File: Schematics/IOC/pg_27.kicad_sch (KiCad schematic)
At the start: 18 parts, among them U2801 F64, U2802 F64, U2803 F74, U2804 F74, U2805 F04, U2806 F04, U2807 F04, U2808 F04, U2809 F04, U2810 F04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

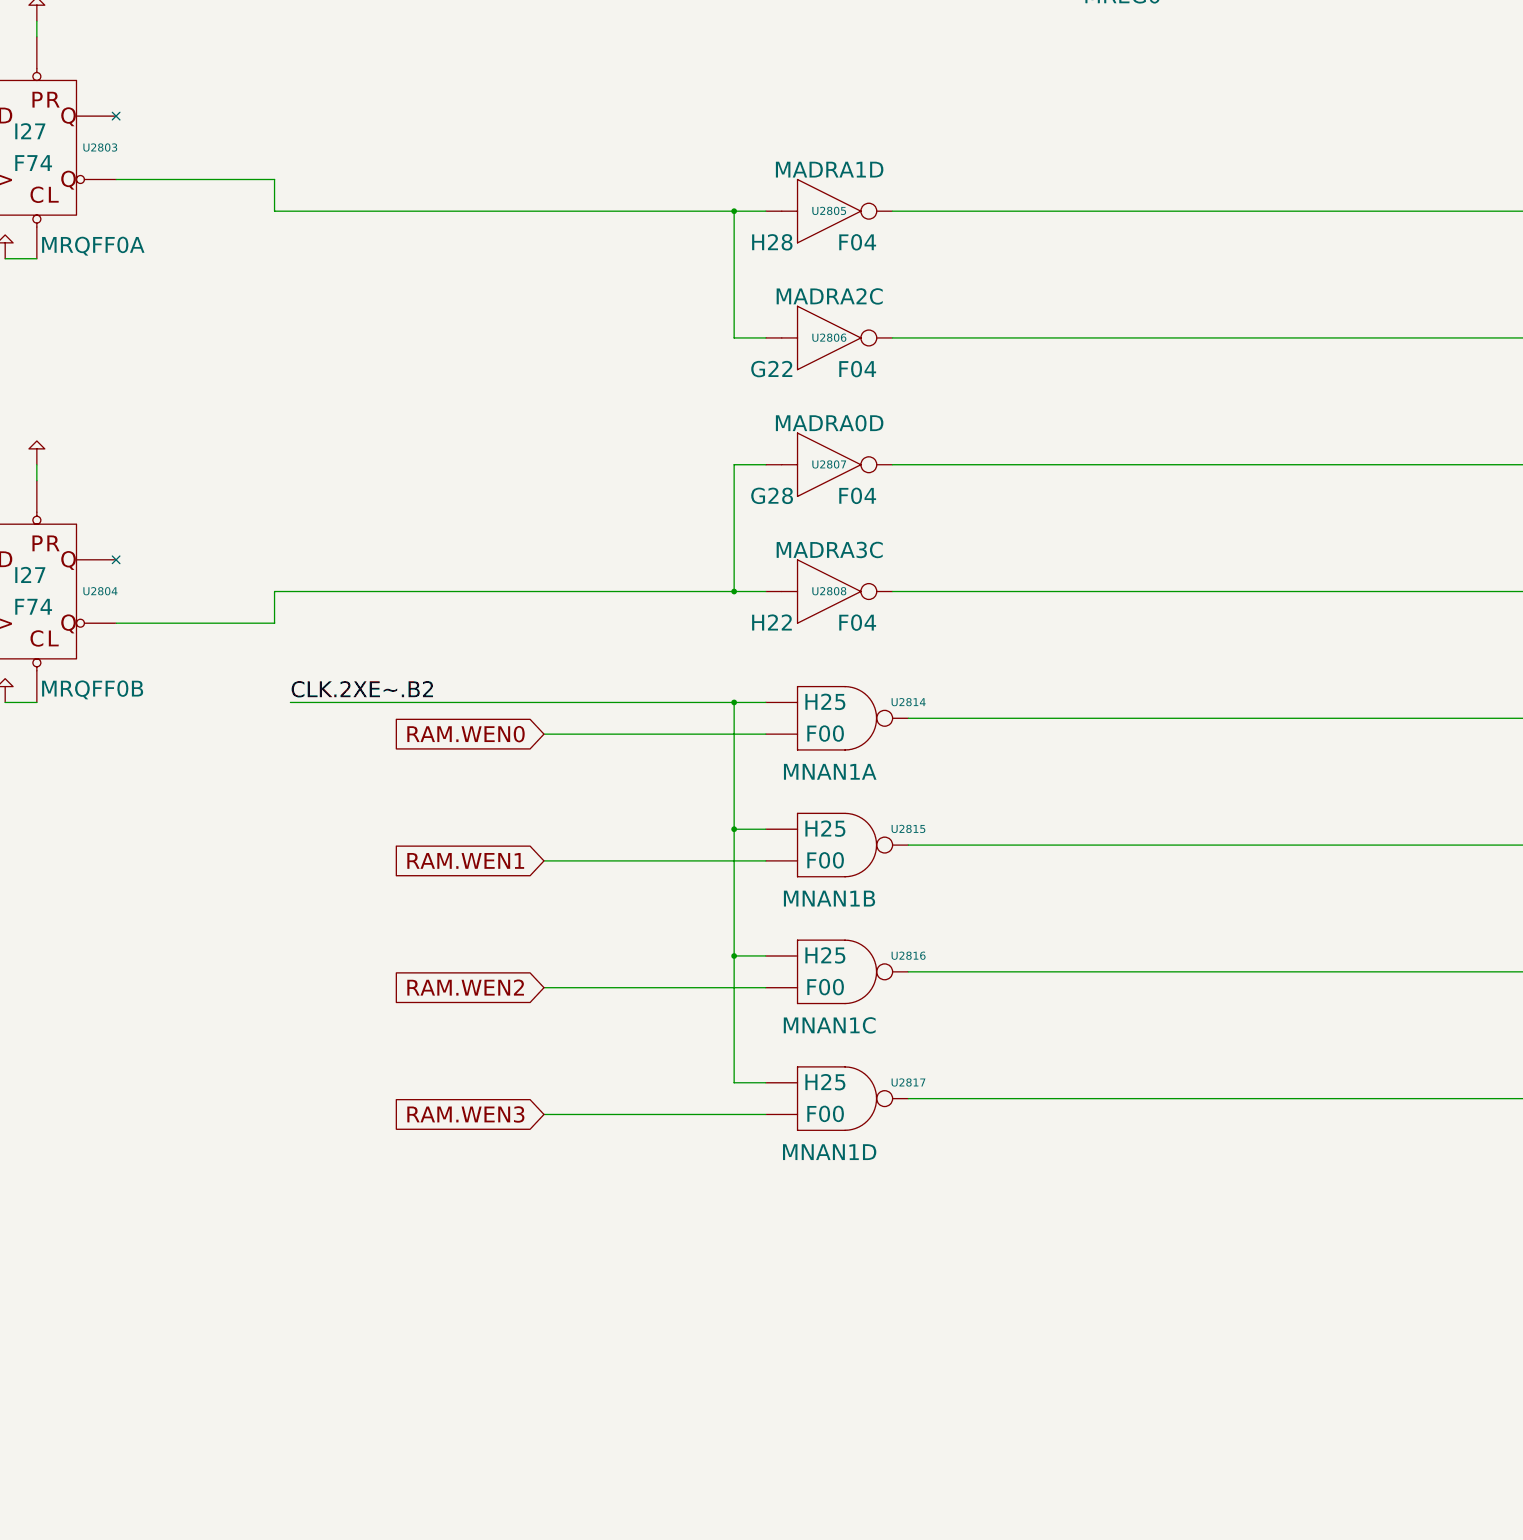
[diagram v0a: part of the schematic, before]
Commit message: Add workarounds necessary for SystemC simulation.
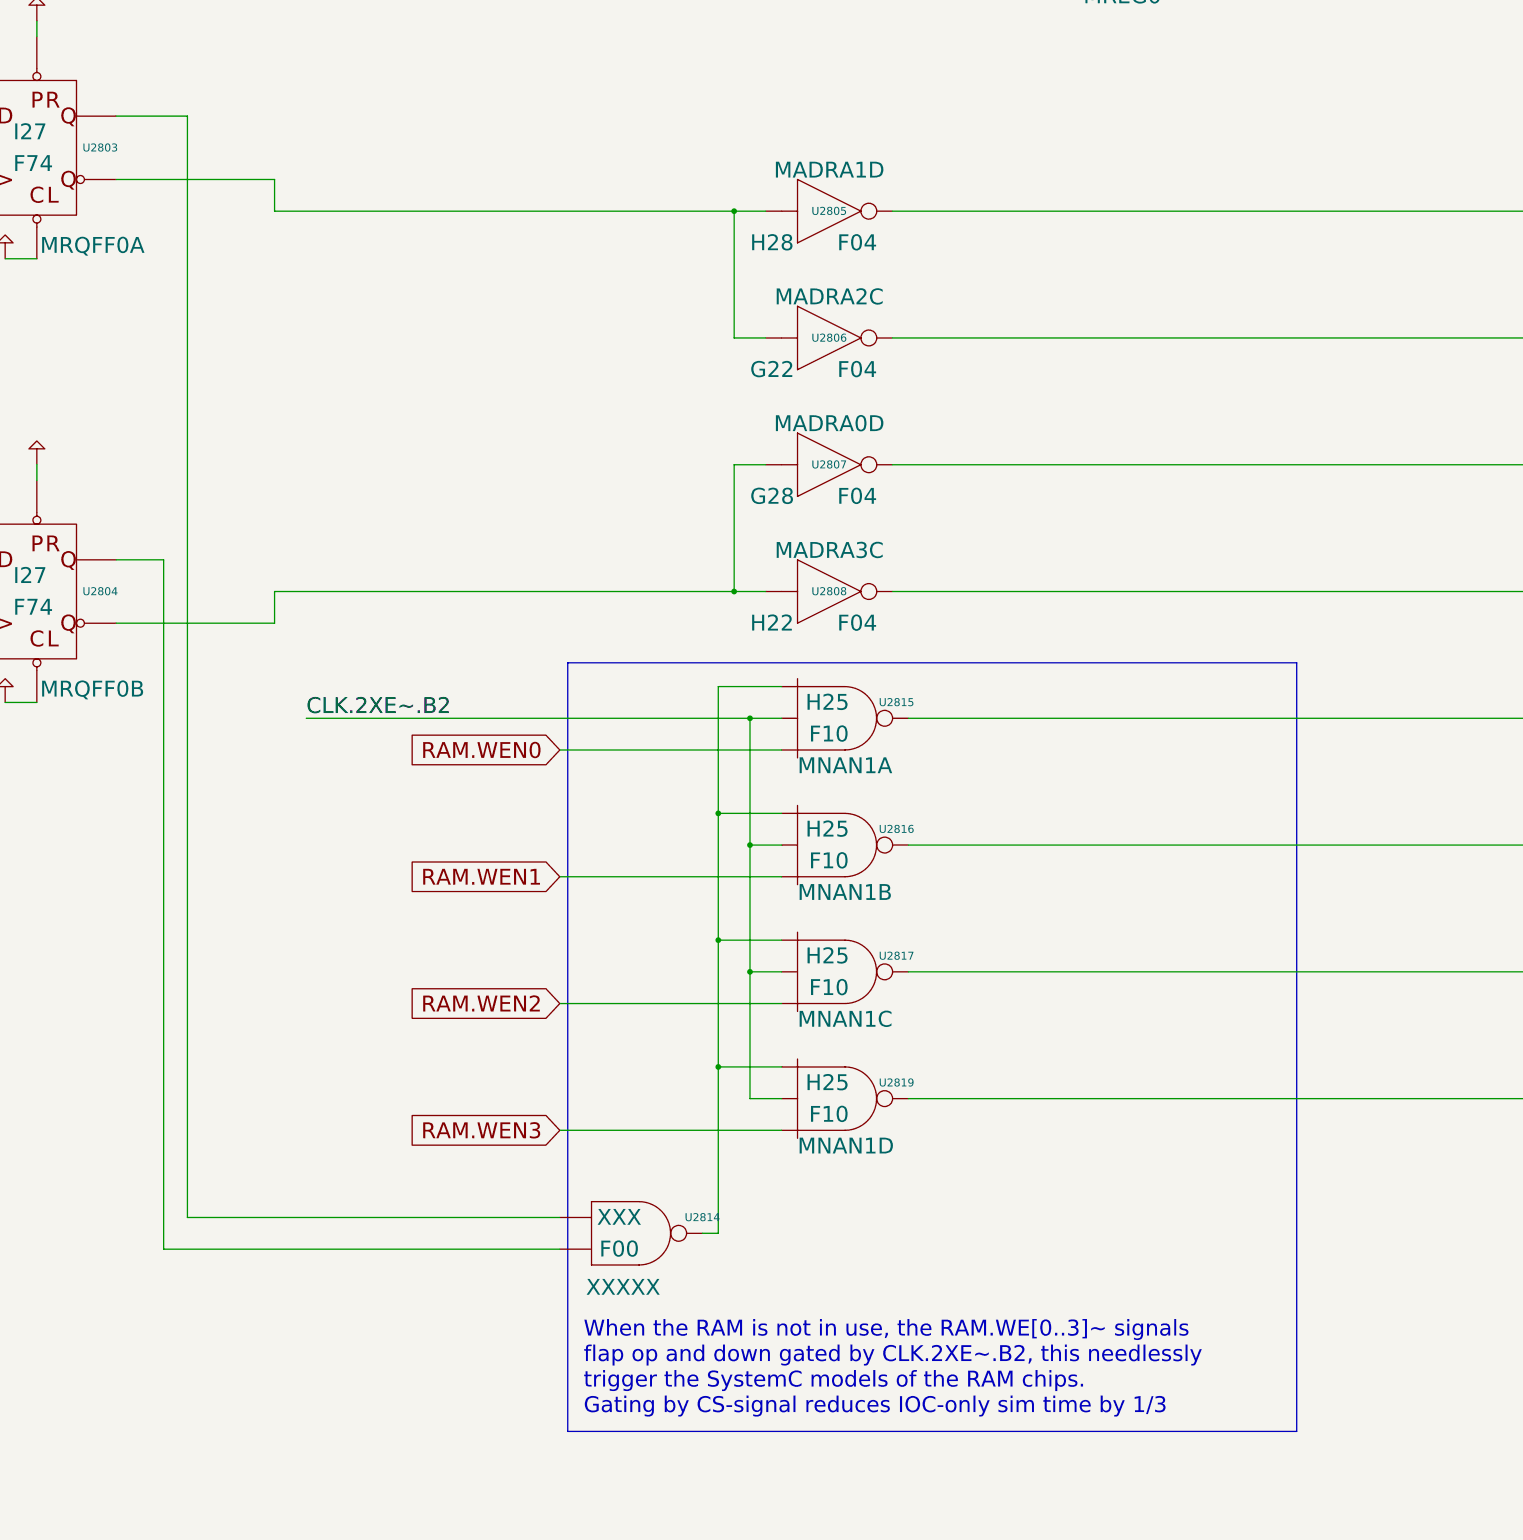
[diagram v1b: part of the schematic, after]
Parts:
- removed U2815, U2816, U2817: F00, symbol r1000:F00
- added U2815, U2816, U2817, U2819: F10, symbol r1000:F10
- U2814: Location H25 -> XXX; Name MNAN1A -> XXXXX
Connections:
- net CLK.2XE~.B2: now also U2815.2 (D1), U2816.2 (D1), U2817.2 (D1), U2819.2 (D1); no longer U2814.1 (D0)
- net RAM.WE0~: now also U2815.4 (Q); no longer U2814.3 (Q)
- net RAM.WE1~: now also U2816.4 (Q)
- net RAM.WE2~: now also U2817.4 (Q)
- net RAM.WE3~: now also U2819.4 (Q)
- net RAM.WEN0: now also U2815.3 (D2); no longer U2814.2 (D1)
- net RAM.WEN1: now also U2816.3 (D2)
- net RAM.WEN2: now also U2817.3 (D2)
- net RAM.WEN3: now also U2819.3 (D2)
- net at U2803.5 (Q): now also U2814.1 (D0)
- net at U2804.5 (Q): now also U2814.2 (D1)
- new net: U2814.3 (Q), U2815.1 (D0), U2816.1 (D0), U2817.1 (D0), U2819.1 (D0)
- no-connect marks 6 -> 4
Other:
- note added: "When the RAM is not in use, the RAM.WE[0..3]~ signals flap op and down gated by CLK.2XE~.B2, this needlessly trigger the SystemC models of the RAM chips. Gating by CS-signal reduces IOC-only sim time by 1/3"

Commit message: Eliminate all multi-buffered signals
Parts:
- removed U2806, U2807: F04, symbol r1000:F04
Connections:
- net RAM.CS1.B1~ is gone; now on net RAM.CS1.B0~: U2808.2 (Q)
- net CLK.2X.B5 renamed CLK.2X.B0
- net CLK.2XE~.B2 renamed CLK.2XE~.B0
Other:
- note added: "When the RAM is not in use, the RAM.WE[0..3]~ signals flap op and down gated by CLK.2XE~.B0, this needlessly trigger the SystemC models of the RAM chips. Gating by CS-signal reduces IOC-only sim time by 1/3"
- note removed: "When the RAM is not in use, the RAM.WE[0..3]~ signals flap op and down gated by CLK.2XE~.B2, this needlessly trigger the SystemC models of the RAM chips. Gating by CS-signal reduces IOC-only sim time by 1/3"

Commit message: Replace lots of clock-generation logic with CLKGEN
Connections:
- net CLK.2X.B0 renamed BP.2X.B0
- net CLK.2XE~.B0 renamed BP.2X~.B0
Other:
- note added: "When the RAM is not in use, the RAM.WE[0..3]~ signals flap op and down gated by BP.2X~.B0, this needlessly trigger the SystemC models of the RAM chips. Gating by CS-signal reduces IOC-only sim time by 1/3"
- note removed: "When the RAM is not in use, the RAM.WE[0..3]~ signals flap op and down gated by CLK.2XE~.B0, this needlessly trigger the SystemC models of the RAM chips. Gating by CS-signal reduces IOC-only sim time by 1/3"
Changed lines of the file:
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@@
   )
   (text
-    "When the RAM is not in use, the RAM.WE[0..3]~ signals\nflap op and down gated by CLK.2XE~.B0, this needlessly\ntrigger the SystemC models of the RAM chips.\nGating by CS-signal reduces IOC-only sim time by 1/3"
+    "When the RAM is not in use, the RAM.WE[0..3]~ signals\nflap op and down gated by BP.2X~.B0, this needlessly\ntrigger the SystemC models of the RAM chips.\nGating by CS-signal reduces IOC-only sim time by 1/3"
     (at 265.43 347.98 0)
     (effects
@@
   )
   (label
-    "CLK.2XE~.B0"
+    "BP.2X~.B0"
     (at 220.98 236.22 0)
     (effects
@@
   )
   (label
-    "CLK.2X.B0"
+    "BP.2X.B0"
     (at 139.7 149.86 0)
     (effects
@@
   )
   (label
-    "CLK.2X.B0"
+    "BP.2X.B0"
     (at 320.04 50.8 0)
     (effects
@@
   )
   (label
-    "CLK.2X.B0"
+    "BP.2X.B0"
     (at 139.7 220.98 0)
     (effects
@@
   )
   (global_label
-    "CLK.2X.B0"
+    "BP.2X.B0"
     (shape input)
     (at 58.42 38.1 180)
@@
   )
   (global_label
-    "CLK.2XE~.B0"
+    "BP.2X~.B0"
     (shape input)
     (at 63.5 43.18 180)

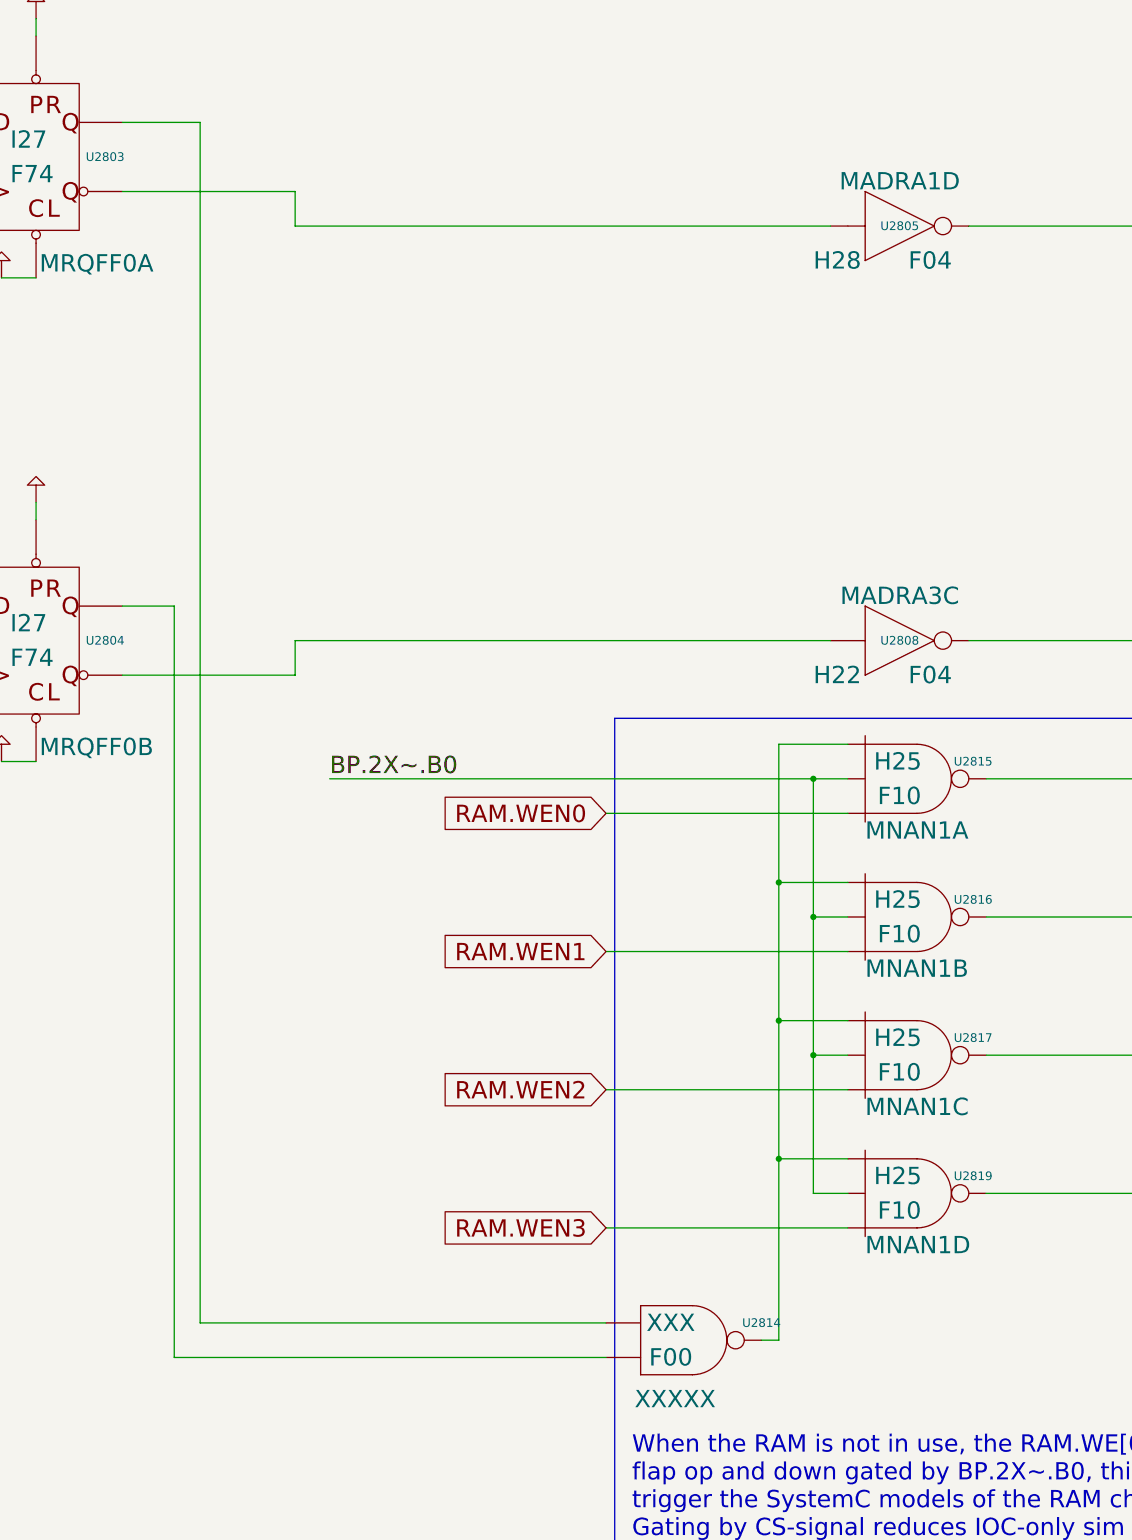
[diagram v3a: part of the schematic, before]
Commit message: Reduce RDNAN[01] and MNAN1 activations
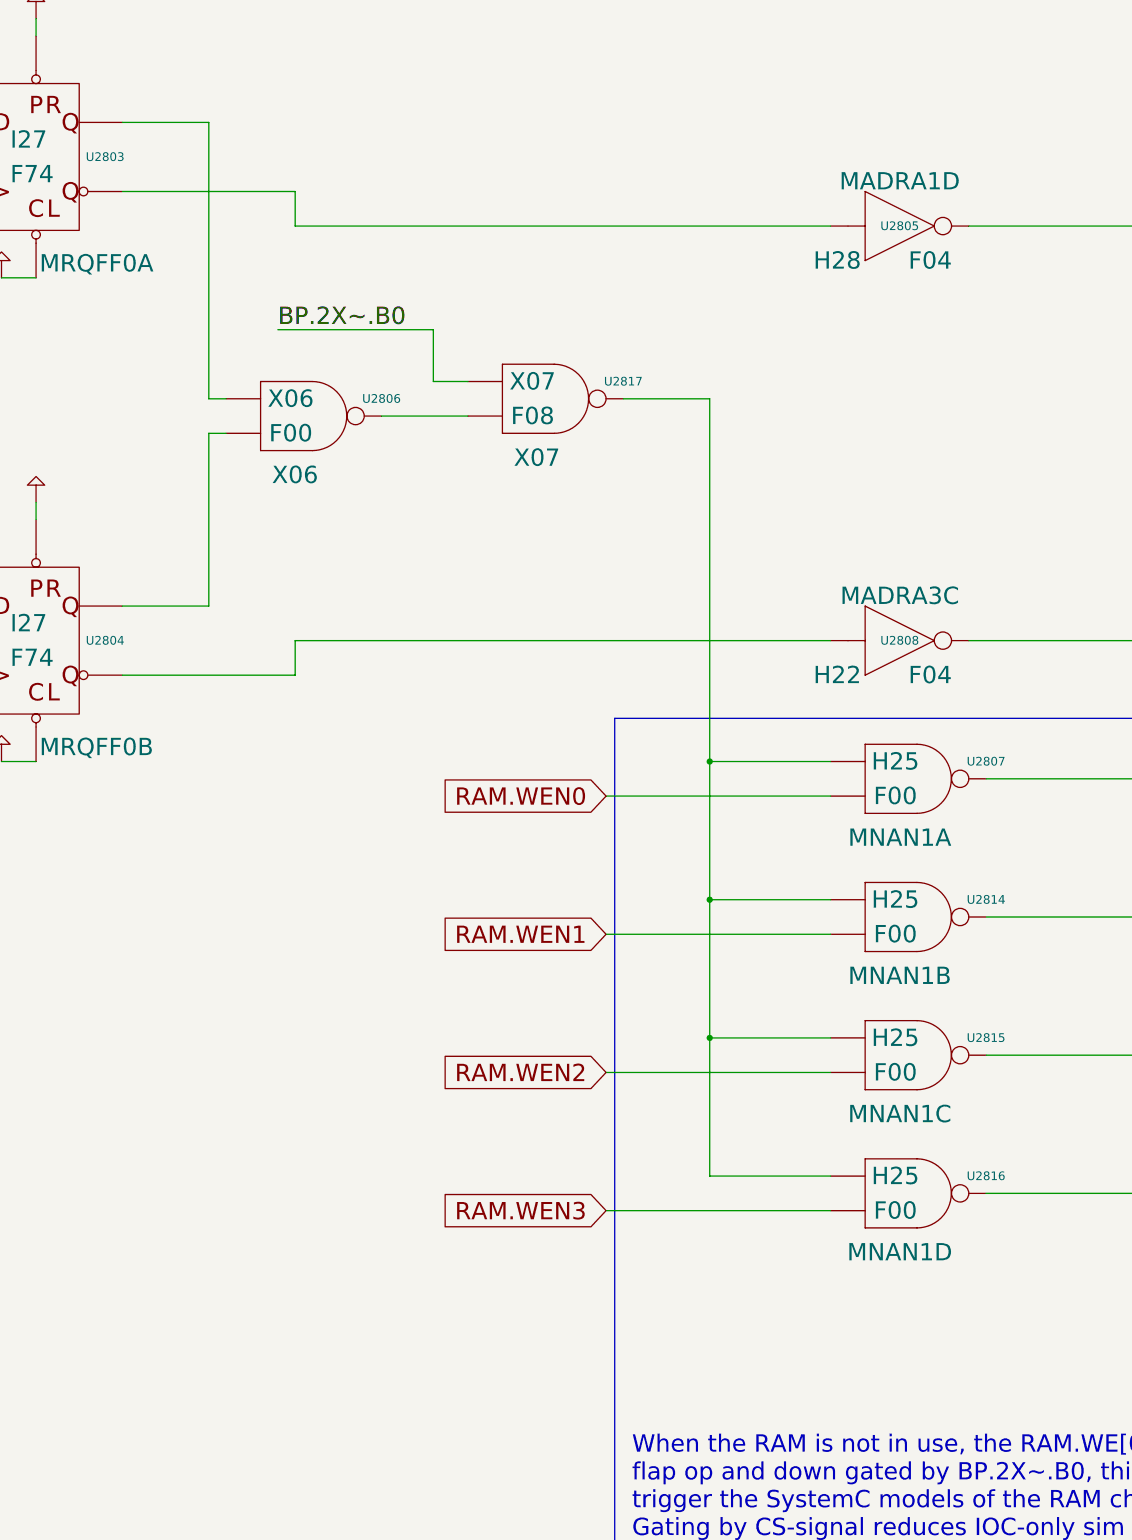
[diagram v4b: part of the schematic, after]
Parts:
- removed U2815, U2816, U2817, U2819: F10, symbol r1000:F10
- added U2806, U2807, U2815, U2816: F00, symbol r1000:F00
- added U2817: F08, symbol r1000:F08
- U2814: Location XXX -> H25; Name XXXXX -> MNAN1B
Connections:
- net BP.2X~.B0: now also U2817.1 (D0)
- net RAM.WE0~: now also U2807.3 (Q)
- net RAM.WE1~: now also U2814.3 (Q)
- net RAM.WE2~: now also U2815.3 (Q)
- net RAM.WE3~: now also U2816.3 (Q)
- net RAM.WEN0: now also U2807.2 (D1)
- net RAM.WEN1: now also U2814.2 (D1)
- net RAM.WEN2: now also U2815.2 (D1)
- net RAM.WEN3: now also U2816.2 (D1)
- net at U2803.5 (Q): now also U2806.1 (D0); no longer U2814.1 (D0)
- net at U2804.5 (Q): now also U2806.2 (D1); no longer U2814.2 (D1)
- new net: U2807.1 (D0), U2814.1 (D0), U2815.1 (D0), U2816.1 (D0), U2817.3 (Q)
- new net: U2806.3 (Q), U2817.2 (D1)
